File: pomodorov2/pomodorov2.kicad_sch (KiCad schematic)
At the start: 17 parts, among them J2 TC2050-IDC, J3 Conn_01x08, U1 nRF52832-QFxx, Y1 32MHz, Y2 32.768kHz

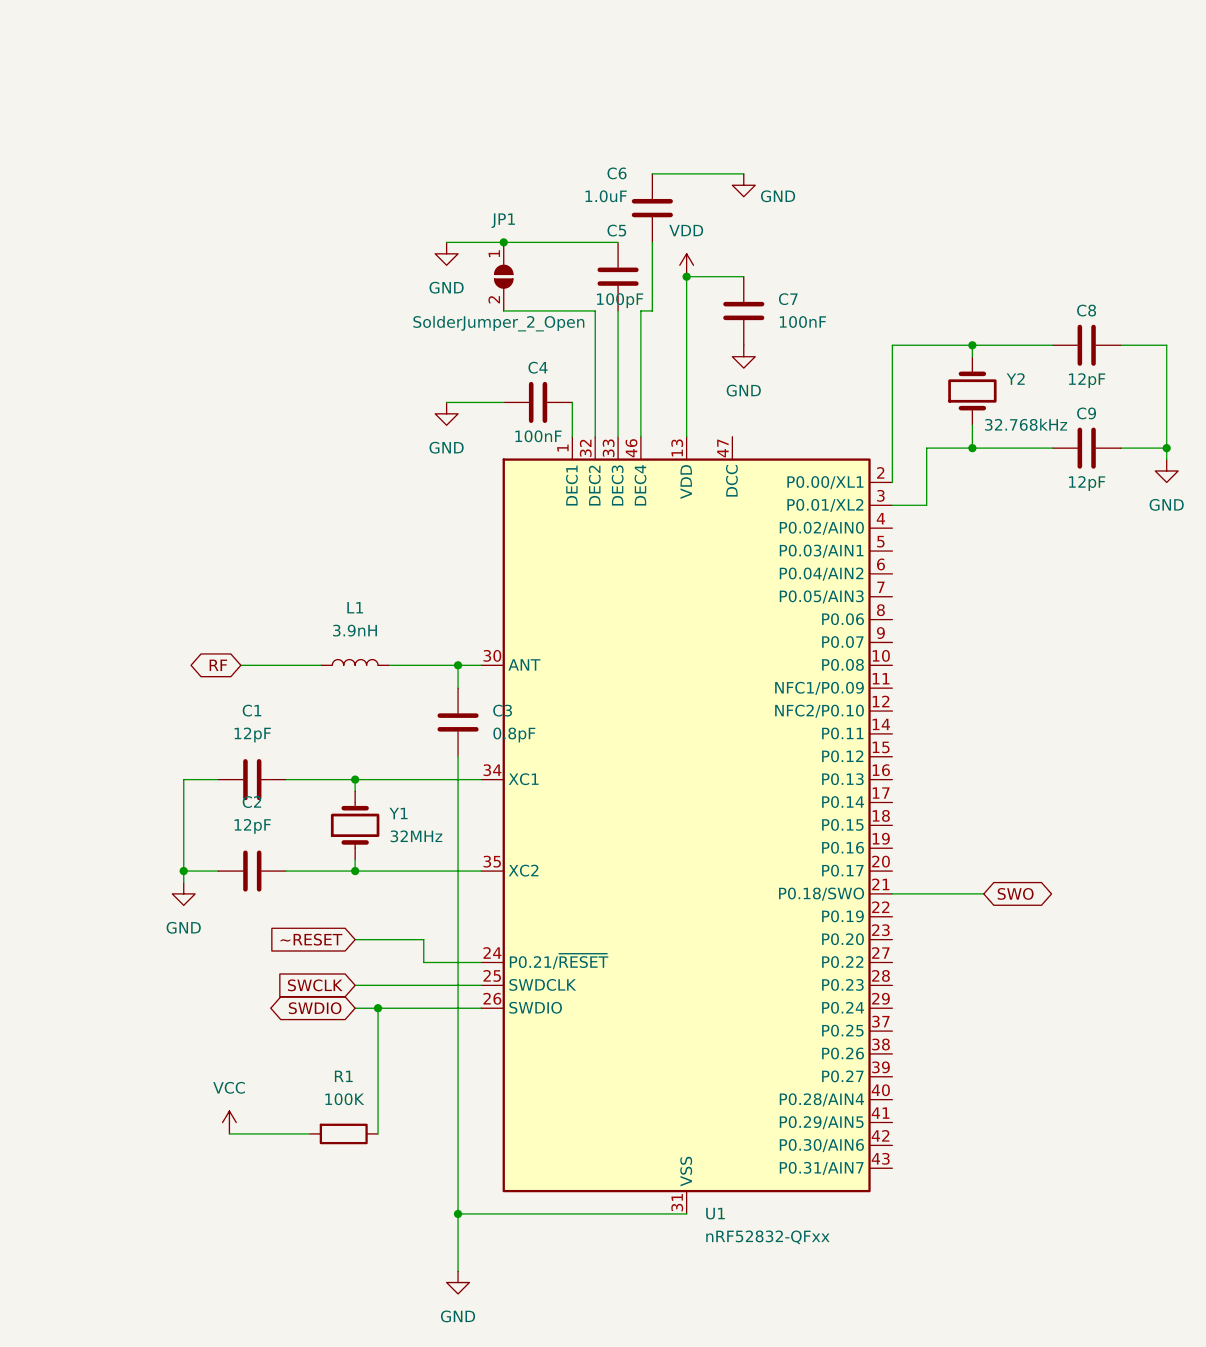
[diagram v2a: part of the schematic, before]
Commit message: Add Adafruit MDBT50Q-1MV2, remove nRF52832 QFN 🔄
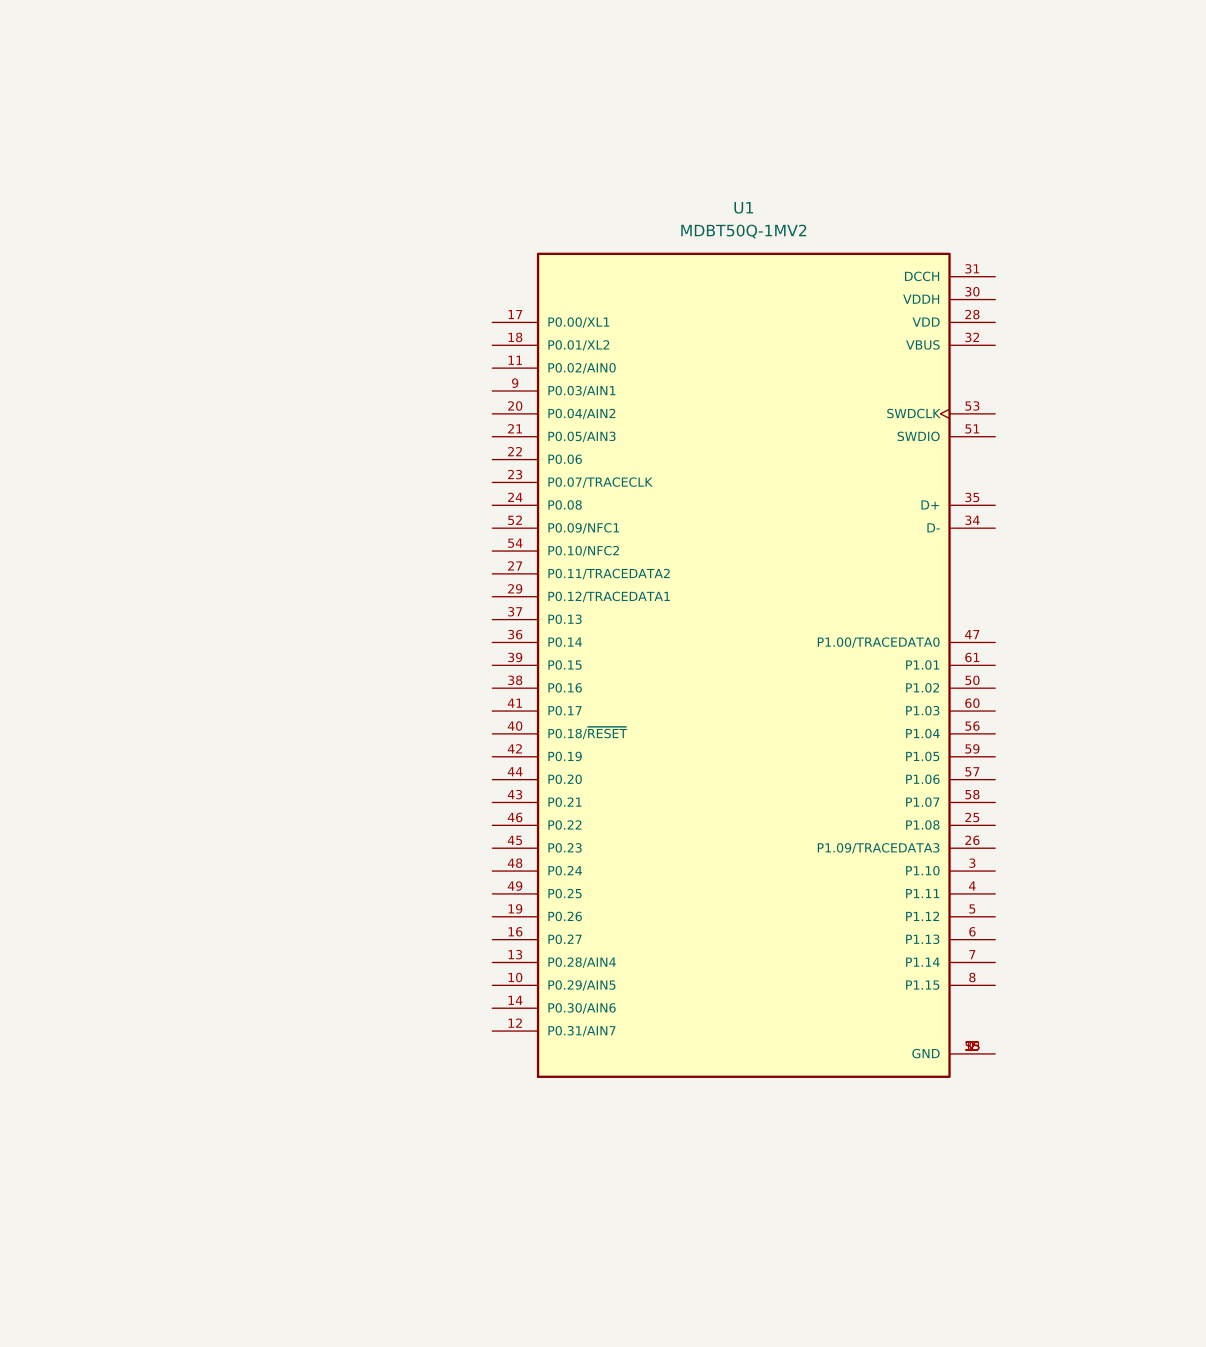
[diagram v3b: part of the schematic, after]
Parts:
- removed C1, C2, C8, C9: 12pF, Capacitor_SMD:C_0805_2012Metric_Pad1.18x1.45mm_HandSolder, symbol Device:C
- removed C3: 0.8pF, Capacitor_SMD:C_0805_2012Metric_Pad1.18x1.45mm_HandSolder, symbol Device:C
- removed C4, C7: 100nF, Capacitor_SMD:C_0805_2012Metric_Pad1.18x1.45mm_HandSolder, symbol Device:C
- removed C5: 100pF, Capacitor_SMD:C_0805_2012Metric_Pad1.18x1.45mm_HandSolder, symbol Device:C
- removed C6: 1.0uF, Capacitor_SMD:C_0805_2012Metric_Pad1.18x1.45mm_HandSolder, symbol Device:C
- removed JP1: SolderJumper_2_Open, Jumper:SolderJumper-2_P1.3mm_Open_TrianglePad1.0x1.5mm, symbol Jumper:SolderJumper_2_Open
- removed L1: 3.9nH, Inductor_SMD:L_0805_2012Metric_Pad1.15x1.40mm_HandSolder, symbol Device:L
- removed R1: 100K, Resistor_SMD:R_0805_2012Metric_Pad1.20x1.40mm_HandSolder, symbol Device:R
- removed U1: nRF52832-QFxx, Package_DFN_QFN:QFN-48-1EP_6x6mm_P0.4mm_EP4.6x4.6mm, symbol MCU_Nordic:nRF52832-QFxx
- removed Y1: 32MHz, Crystal:Crystal_SMD_2016-4Pin_2.0x1.6mm, symbol Device:Crystal
- removed Y2: 32.768kHz, Crystal:Crystal_SMD_3215-2Pin_3.2x1.5mm, symbol Device:Crystal
- added U1: MDBT50Q-1MV2, MDBT50Q-1MV2:XCVR_MDBT50Q-1MV2, symbol MDBT50Q-1MV2:MDBT50Q-1MV2
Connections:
- new net: U1.1 (GND), U1.15 (GND), U1.2 (GND), U1.33 (GND), U1.55 (GND)

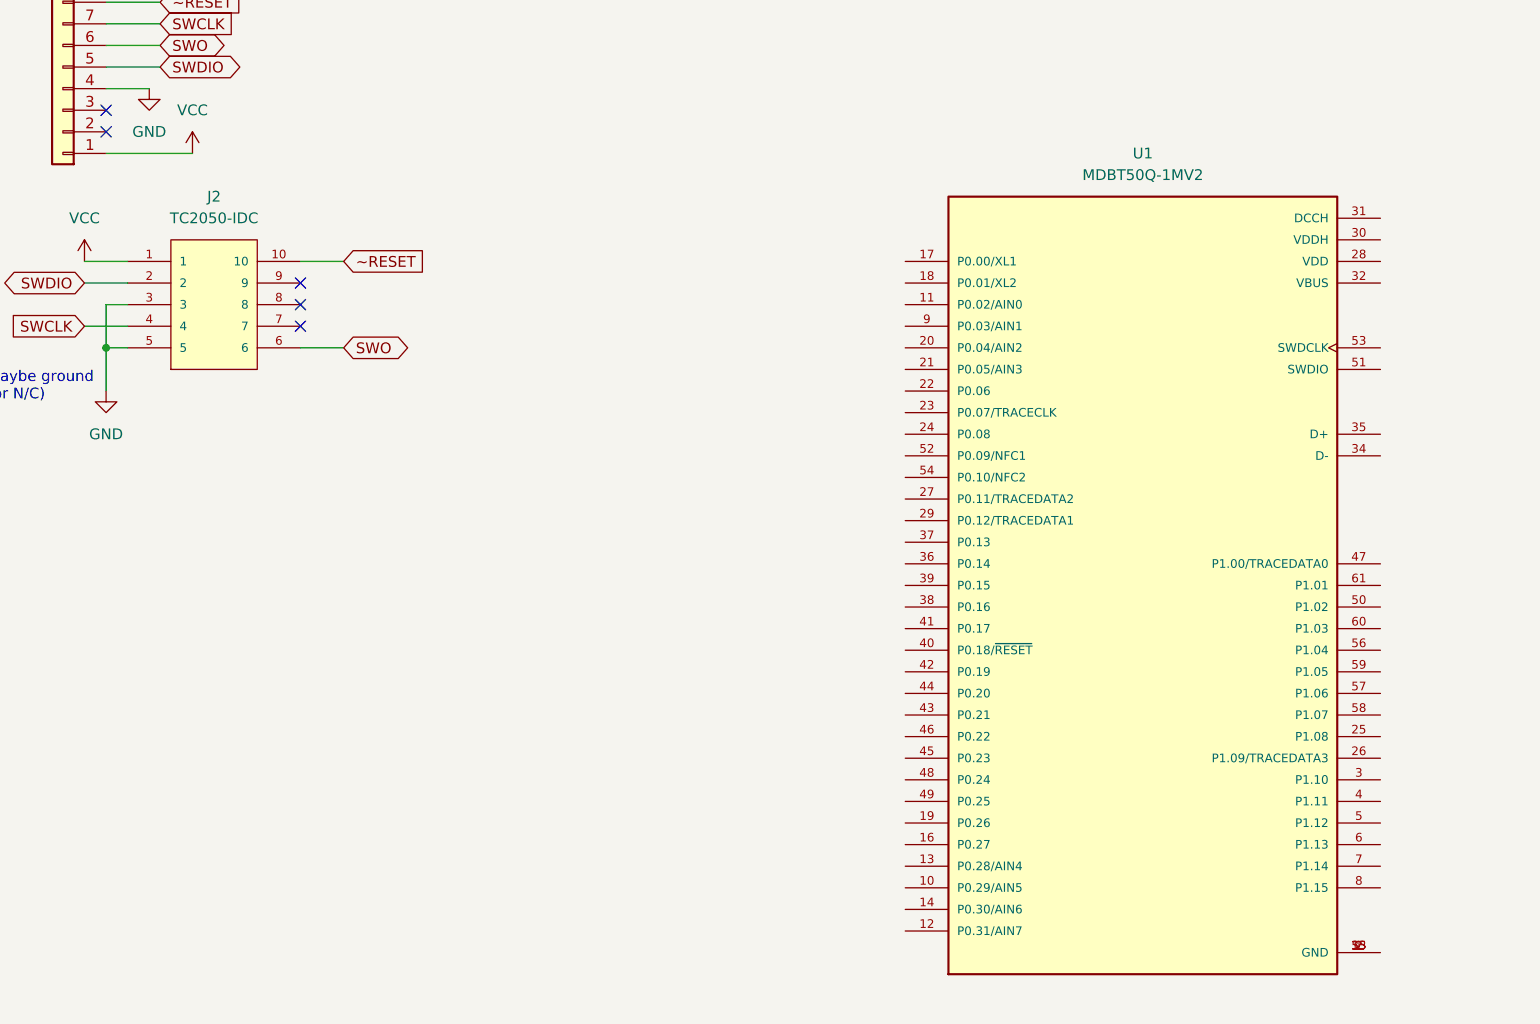
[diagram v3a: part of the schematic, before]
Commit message: Adding test points, usb, crystals 💎
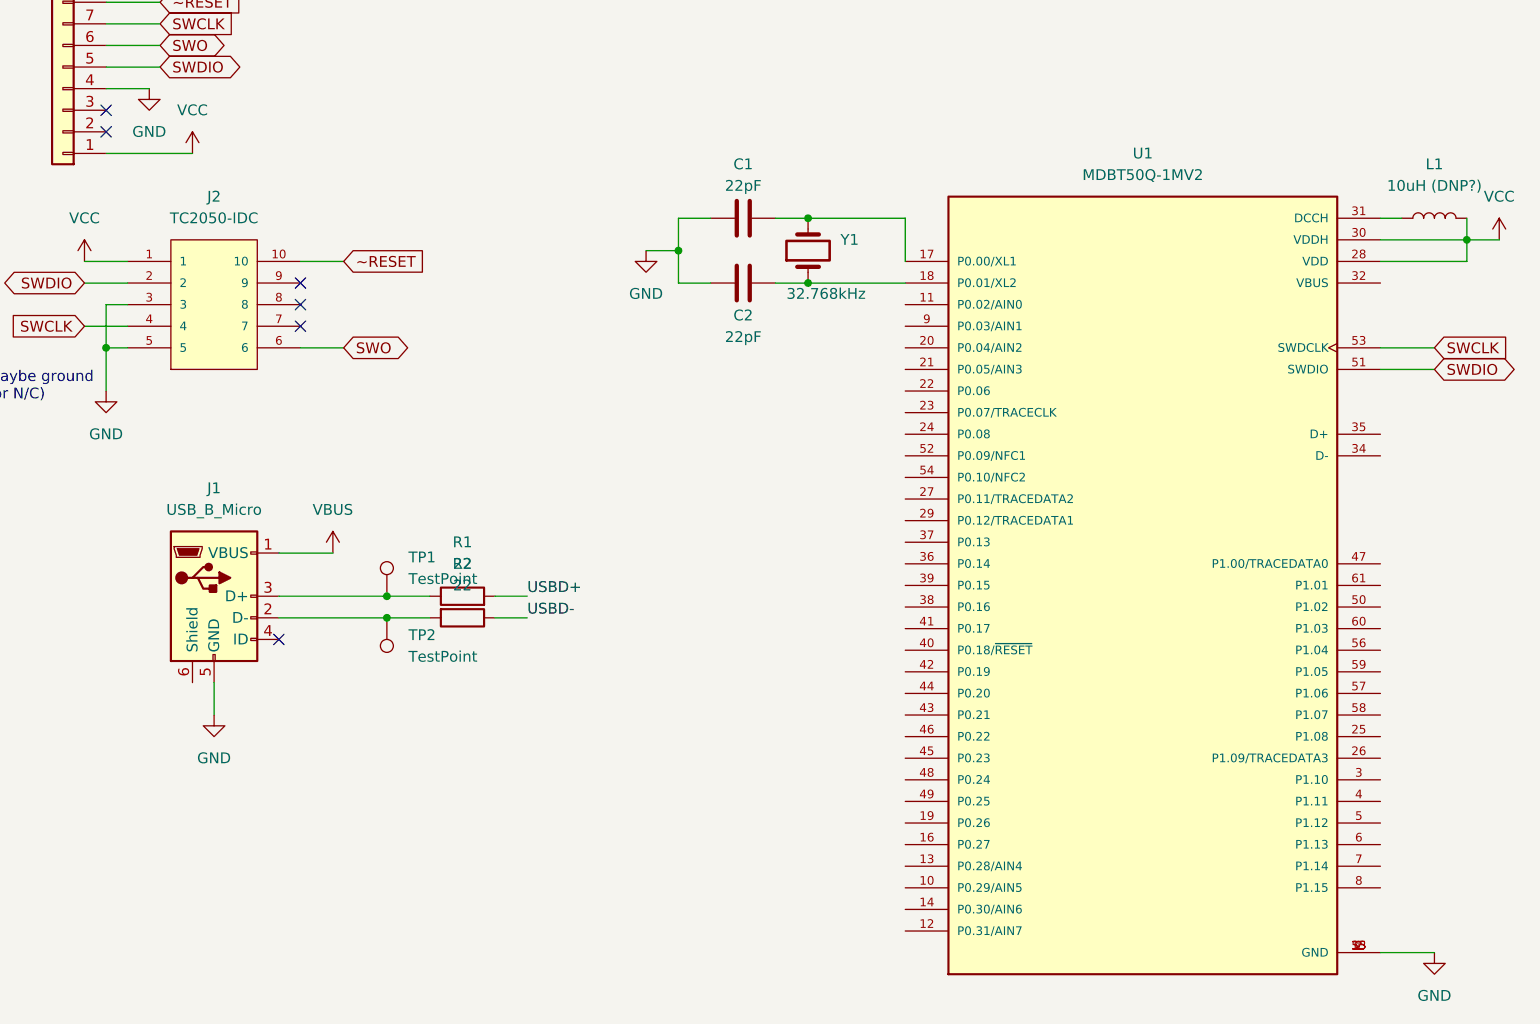
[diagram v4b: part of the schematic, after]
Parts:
- added C1, C2: 22pF, Capacitor_SMD:C_0805_2012Metric_Pad1.18x1.45mm_HandSolder, symbol Device:C
- added J1: USB_B_Micro, Connector_USB:USB_Micro-B_Amphenol_10104110_Horizontal, symbol Connector:USB_B_Micro
- added L1: 10uH (DNP?), Inductor_SMD:L_0805_2012Metric_Pad1.05x1.20mm_HandSolder, symbol Device:L
- added R1, R2: 22, Resistor_SMD:R_0805_2012Metric_Pad1.20x1.40mm_HandSolder, symbol Device:R
- added TP1, TP2: TestPoint, TestPoint:TestPoint_Pad_D1.0mm, symbol Connector:TestPoint
- added Y1: 32.768kHz, Crystal:Crystal_SMD_2012-2Pin_2.0x1.2mm_HandSoldering, symbol Device:Crystal
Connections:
- net GND: now also U1.1 (GND), U1.15 (GND), U1.2 (GND), U1.33 (GND), U1.55 (GND), C1.1, C2.1, J1.5 (GND)
- net SWCLK: now also U1.53 (SWDCLK)
- net SWDIO: now also U1.51 (SWDIO)
- net VCC: now also U1.28 (VDD), U1.30 (VDDH), L1.2
- net at U1.17 (P0.00/XL1): now also C1.2, Y1.2
- net at U1.18 (P0.01/XL2): now also C2.2, Y1.1
- net at U1.31 (DCCH): now also L1.1
- new net: J1.2 (D-), R2.2, TP2.1
- new net: J1.3 (D+), R1.1, TP1.1
- new net USBD+: R1.2
- new net USBD-: R2.1
- new net VBUS: J1.1 (VBUS)
- no-connect marks 5 -> 6

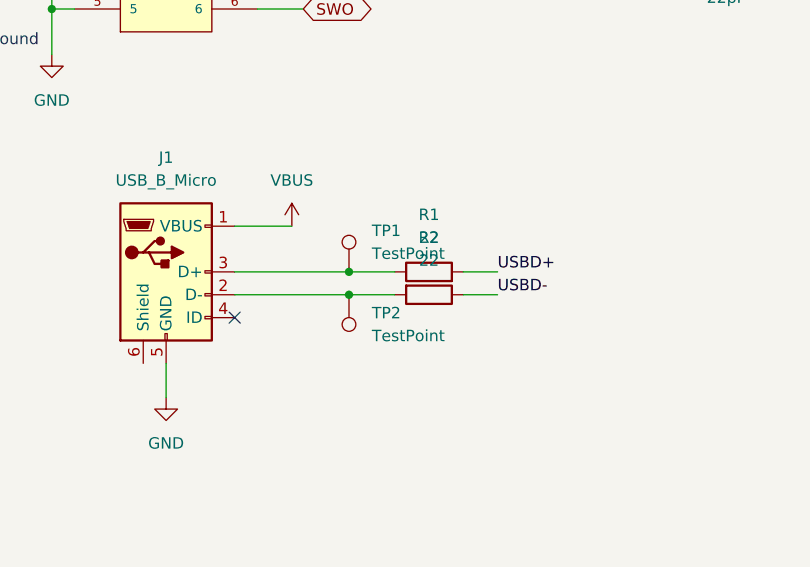
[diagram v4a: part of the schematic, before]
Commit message: Make schematic more legible 👓
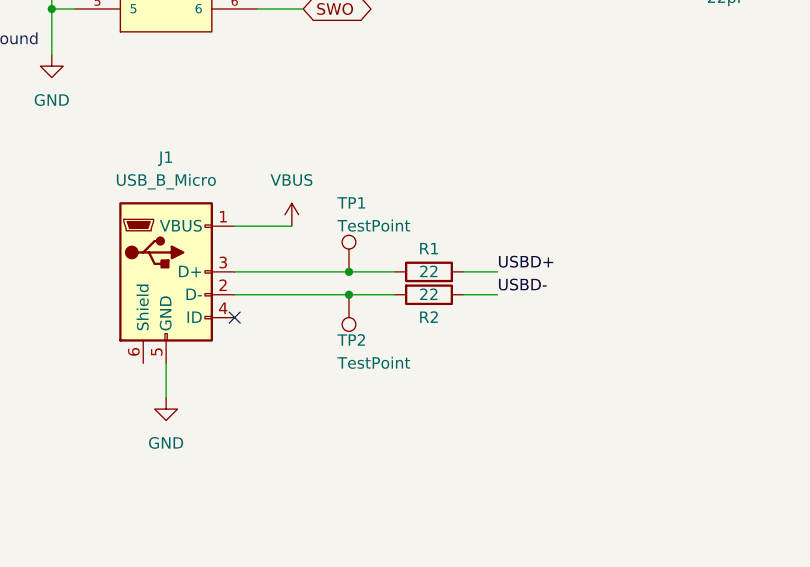
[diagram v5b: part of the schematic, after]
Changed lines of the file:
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@@
   )
   (symbol (lib_id "Device:R") (at 68.58 93.98 270) (unit 1)
-    (in_bom yes) (on_board yes) (fields_autoplaced)
-    (property "Reference" "R2" (id 0) (at 68.58 87.63 90))
-    (property "Value" "22" (id 1) (at 68.58 90.17 90))
+    (in_bom yes) (on_board yes)
+    (property "Reference" "R2" (id 0) (at 68.58 96.52 90))
+    (property "Value" "22" (id 1) (at 68.58 93.98 90))
     (property "Footprint" "Resistor_SMD:R_0805_2012Metric_Pad1.20x1.40mm_HandSolder" (id 2) (at 68.58 92.202 90)
       (effects (font (size 1.27 1.27)) hide)
@@
   )
   (symbol (lib_id "Device:R") (at 68.58 91.44 90) (unit 1)
-    (in_bom yes) (on_board yes) (fields_autoplaced)
-    (property "Reference" "R1" (id 0) (at 68.58 85.09 90))
-    (property "Value" "22" (id 1) (at 68.58 87.63 90))
+    (in_bom yes) (on_board yes)
+    (property "Reference" "R1" (id 0) (at 68.58 88.9 90))
+    (property "Value" "22" (id 1) (at 68.58 91.44 90))
     (property "Footprint" "Resistor_SMD:R_0805_2012Metric_Pad1.20x1.40mm_HandSolder" (id 2) (at 68.58 93.218 90)
       (effects (font (size 1.27 1.27)) hide)
@@
   )
   (symbol (lib_id "Connector:TestPoint") (at 59.69 91.44 0) (unit 1)
-    (in_bom yes) (on_board yes) (fields_autoplaced)
-    (property "Reference" "TP1" (id 0) (at 62.23 86.8679 0)
+    (in_bom yes) (on_board yes)
+    (property "Reference" "TP1" (id 0) (at 58.42 83.82 0)
       (effects (font (size 1.27 1.27)) (justify left))
     )
-    (property "Value" "TestPoint" (id 1) (at 62.23 89.4079 0)
+    (property "Value" "TestPoint" (id 1) (at 58.42 86.36 0)
       (effects (font (size 1.27 1.27)) (justify left))
     )
@@
   )
   (symbol (lib_id "Connector:TestPoint") (at 59.69 93.98 180) (unit 1)
-    (in_bom yes) (on_board yes) (fields_autoplaced)
-    (property "Reference" "TP2" (id 0) (at 62.23 96.0119 0)
+    (in_bom yes) (on_board yes)
+    (property "Reference" "TP2" (id 0) (at 58.42 99.06 0)
       (effects (font (size 1.27 1.27)) (justify right))
     )
-    (property "Value" "TestPoint" (id 1) (at 62.23 98.5519 0)
+    (property "Value" "TestPoint" (id 1) (at 58.42 101.6 0)
       (effects (font (size 1.27 1.27)) (justify right))
     )

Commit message: A little routing and schematic cleanup 🧹
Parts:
- J3: value Conn_01x08 -> SOICbite
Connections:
- net USBD+: now also U1.35 (D+)
- net USBD-: now also U1.34 (D-)
- net ~RESET: now also U1.40 (P0.18/~{RESET})
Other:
- note added: "SOICbite debug header"
- note added: "TODO: ground shield?"
- note added: "Tag-connect debug header"
- note added: "USB"
- moved on the sheet: J1, J2, R1, R2, TP1, TP2

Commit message: Some layout, schematic work 👷‍♂️
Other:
- note added: "1"
- note added: "April 10, 2022"
- note added: "Pomodoro Timer V2"
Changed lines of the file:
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@@
+    (effects (font (size 1.27 1.27)) (justify left bottom))
+  )
+  (text "April 10, 2022" (at 207.01 194.31 0)
     (effects (font (size 1.27 1.27)) (justify left bottom))
   )
@@
     (effects (font (size 1.27 1.27)) (justify right bottom))
   )
+  (text "1" (at 269.24 194.31 0)
+    (effects (font (size 1.27 1.27)) (justify left bottom))
+  )
+  (text "Pomodoro Timer V2" (at 186.69 191.77 0)
+    (effects (font (size 2 2)) (justify left bottom))
+  )
   (text "SOICbite\ndebug header" (at 35.56 16.51 0)
